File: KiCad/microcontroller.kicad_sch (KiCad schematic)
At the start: 11 parts, among them J1 Debugger, SW1 Reset switch, U1 STM32F051C6Tx, U7 24LC256

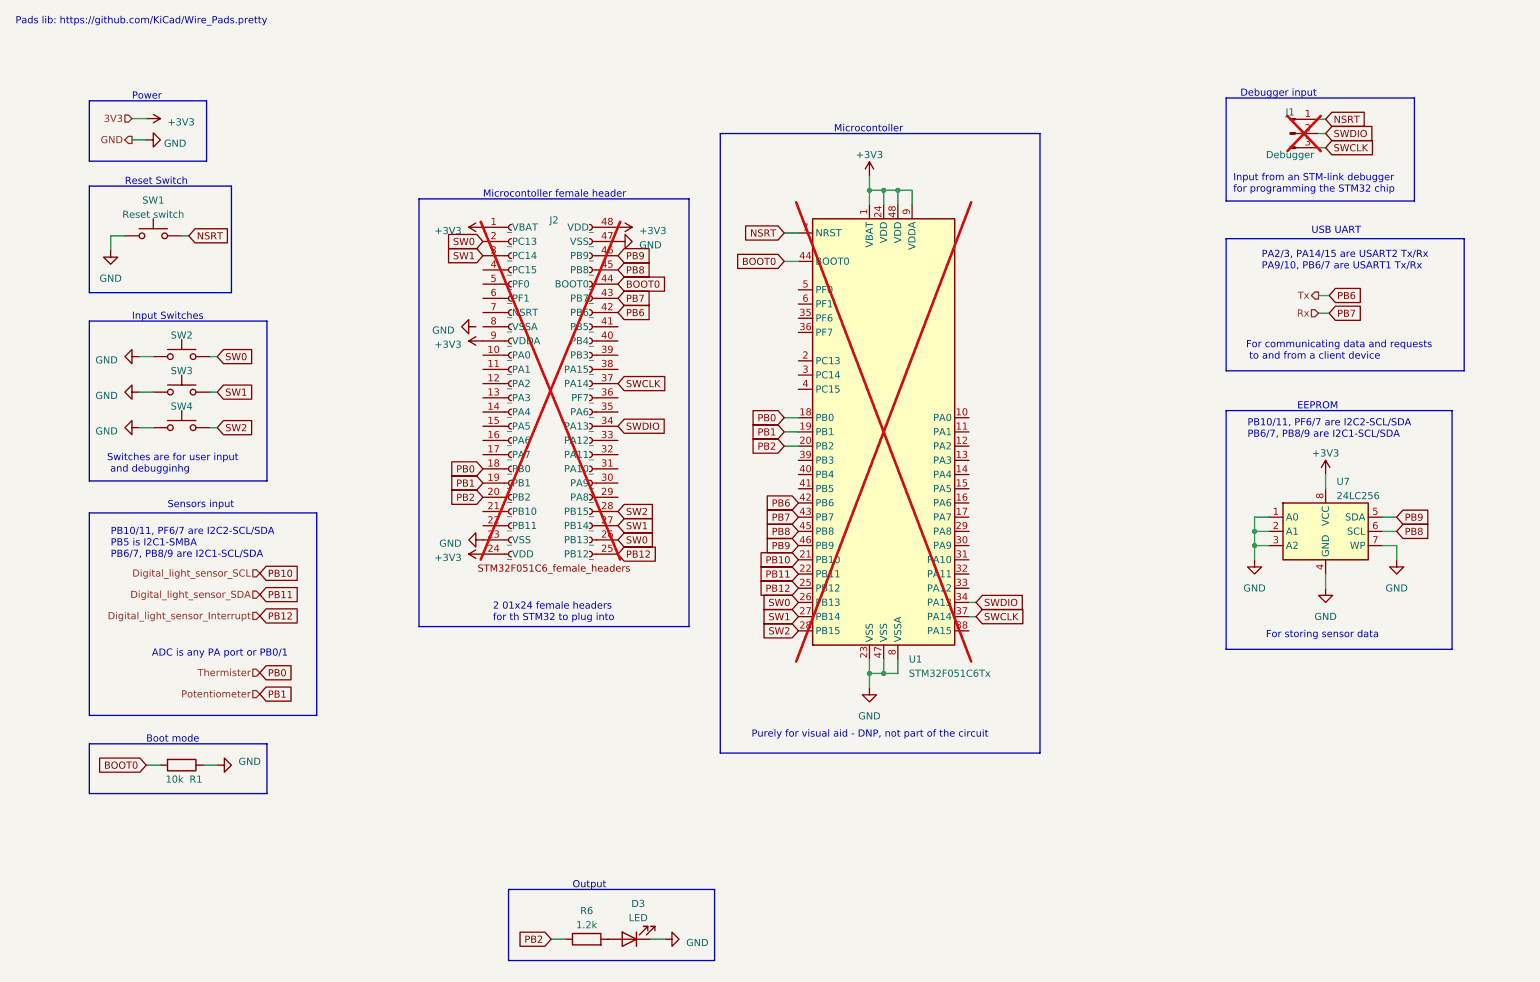
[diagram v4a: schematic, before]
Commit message: added failure mitigations and updated BOM
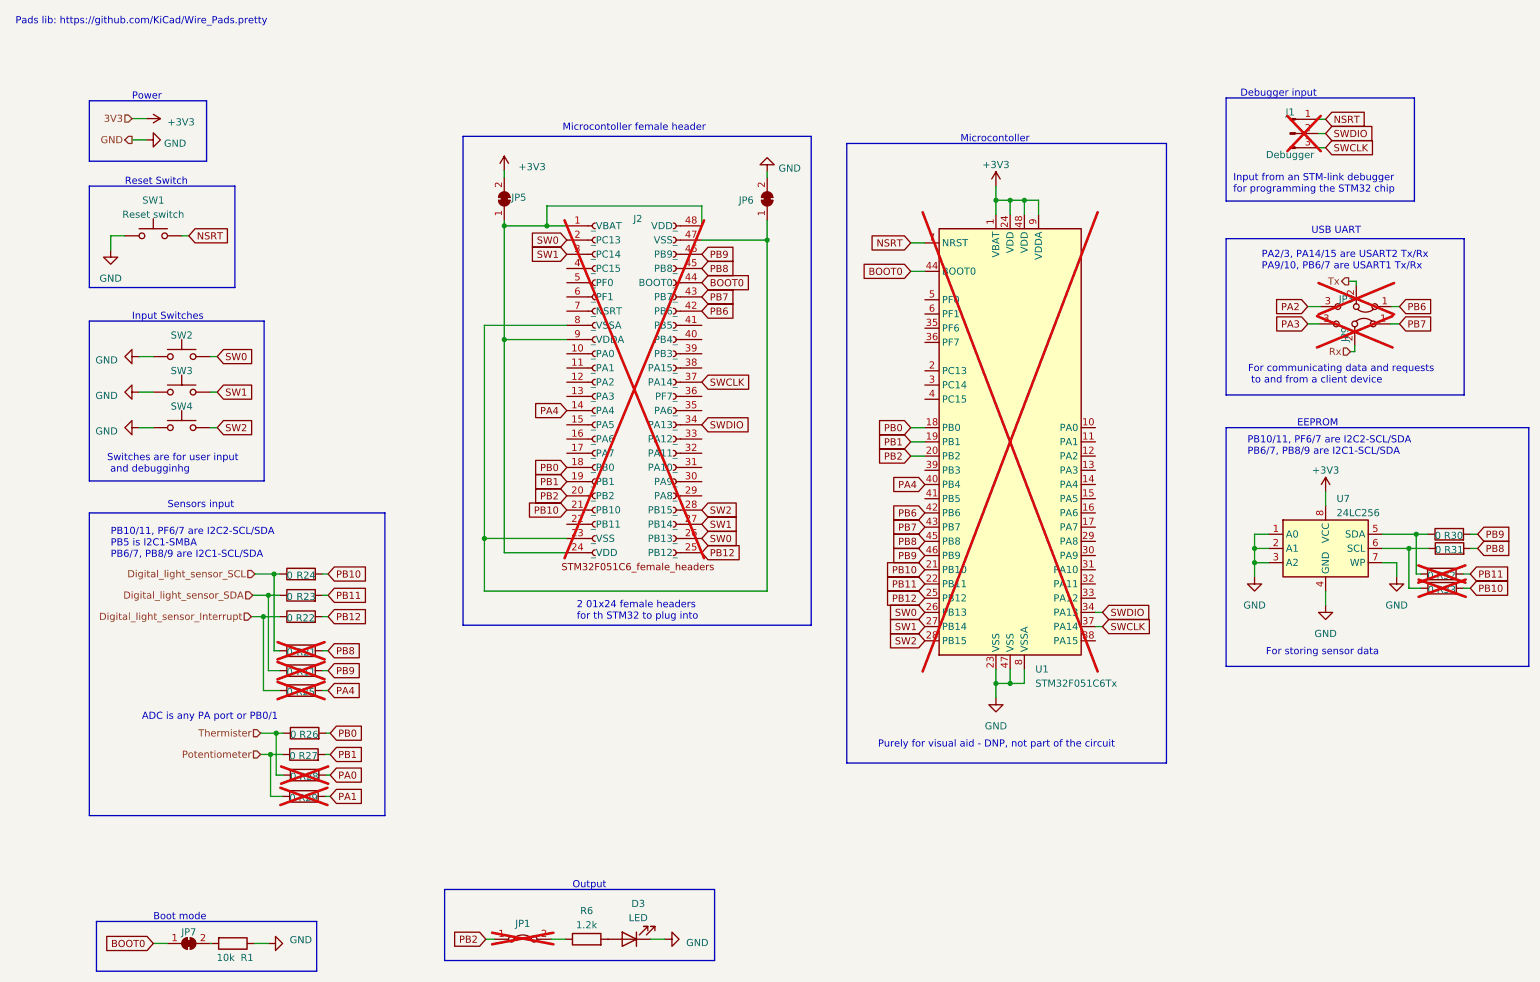
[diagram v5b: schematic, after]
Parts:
- added JP1: Jumper_2_Bridged, symbol Jumper:Jumper_2_Bridged
- added JP3, JP9: Jumper_3_Bridged12, symbol Jumper:Jumper_3_Bridged12
- added JP5, JP6, JP7: SolderJumper_2_Bridged, symbol Jumper:SolderJumper_2_Bridged
- added R11, R21, R22, R23, R24, R25, R26, R27, R28, R29, R30, R31, R32, R33: 0, symbol Device:R
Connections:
- net +3V3: now also JP5.2 (B); no longer J2.1 (_VBAT), J2.24 (_VDD), J2.48 (VDD_), J2.9 (_VDDA)
- net BOOT0: now also JP7.1 (A); no longer R1.2
- net GND: now also JP6.2 (B); no longer J2.23 (_VSS), J2.47 (VSS_)
- net PB0: now also R26.2
- net PB1: now also R27.2
- net PB10: now also J2.21 (_PB10), R24.2, R33.2
- net PB11: now also R23.2, R32.2
- net PB12: now also R22.2
- net PB2: now also JP1.1 (A); no longer R6.1
- net PB6: now also JP3.1 (A)
- net PB7: now also JP9.1 (A)
- net PB8: now also R21.2, R31.2; no longer U7.6 (SCL)
- net PB9: now also R11.2, R30.2; no longer U7.5 (SDA)
- net PA4: now reaches J2.14 (_PA4)
- net PA4: now also U1.40 (PB4), R25.2
- net at J2.8 (_VSSA): now also J2.23 (_VSS), J2.47 (VSS_), JP6.1 (A)
- new net: JP1.2 (B), R6.1
- new net: JP7.2 (B), R1.2
- new net: R30.1, R32.1, U7.5 (SDA)
- new net: R31.1, R33.1, U7.6 (SCL)
- new net: J2.1 (_VBAT), J2.24 (_VDD), J2.48 (VDD_), J2.9 (_VDDA), JP5.1 (A)
- new net Digital_light_sensor_Interrupt: R22.1, R25.1
- new net Digital_light_sensor_SCL: R21.1, R24.1
- new net Digital_light_sensor_SDA: R11.1, R23.1
- new net PA0: R28.2
- new net PA1: R29.2
- new net PA2: JP3.3 (B)
- new net PA3: JP9.3 (B)
- new net Potentiometer: R27.1, R29.1
- new net Rx: JP9.2 (C)
- new net Thermister: R26.1, R28.1
- new net Tx: JP3.2 (C)
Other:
- moved on the sheet: J2, R1, U1, U7

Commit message: updated sensor and microcontroller schematics
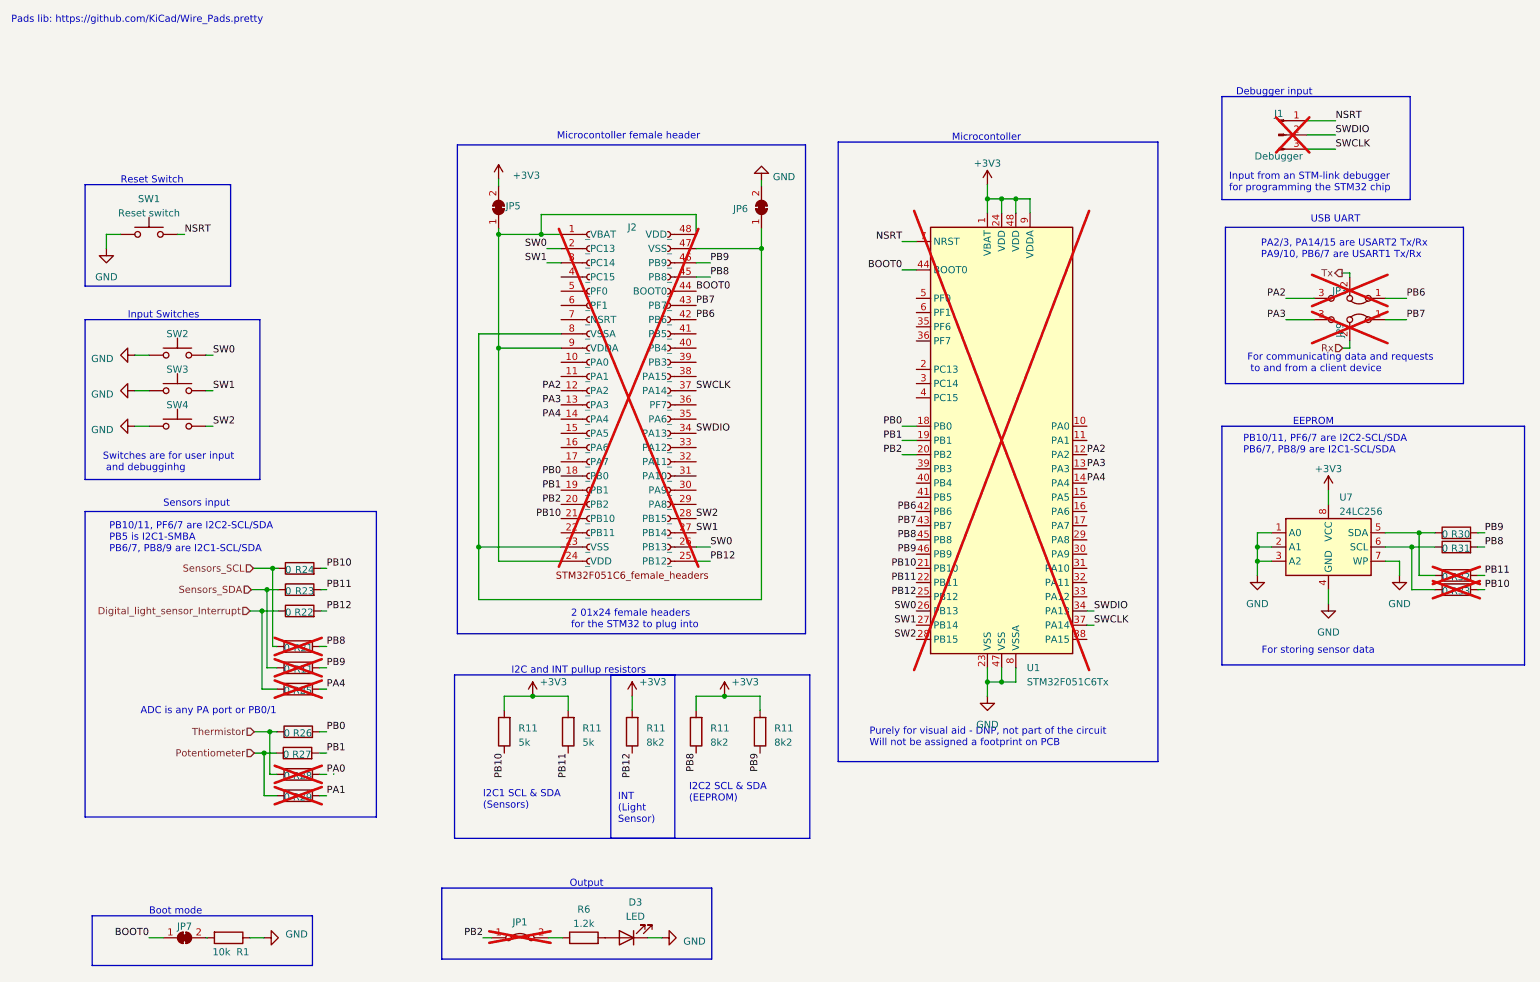
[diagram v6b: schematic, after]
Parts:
- added R11 (x2): 5k, symbol Device:R
- added R11 (x3): 8k2, symbol Device:R
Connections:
- net +3V3: now also R11.2, R11.2, R11.2, R11.2, R11.2
- net PA2: now also J2.12 (_PA2), U1.12 (PA2)
- net PA3: now also J2.13 (_PA3), U1.13 (PA3)
- net PA4: now also U1.14 (PA4); no longer U1.40 (PB4)
- net PB1: no longer R27.2
- net PB10: now also R11.1
- net PB11: now also R11.1
- net PB12: now also R11.1
- net PB8: now also R11.1
- net PB9: now also R11.1
- net Digital_light_sensor_SCL renamed Sensors_SCL
- net Digital_light_sensor_SDA renamed Sensors_SDA
- net Thermister renamed Thermistor
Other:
- note added: "2 01x24 female headers for the STM32 to plug into"
- note added: "I2C and INT pullup resistors"
- note added: "I2C1 SCL & SDA (Sensors)"
- note added: "I2C2 SCL & SDA (EEPROM)"
- note added: "INT (Light Sensor)"
- note added: "Purely for visual aid - DNP, not part of the circuit Will not be assigned a footprint on PCB"
- note removed: "2 01x24 female headers for th STM32 to plug into"
- note removed: "Power"
- note removed: "Purely for visual aid - DNP, not part of the circuit"
- moved on the sheet: D3, J1, J2, JP1, JP3, JP5, JP6, JP7, JP9, R1, R11, R21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

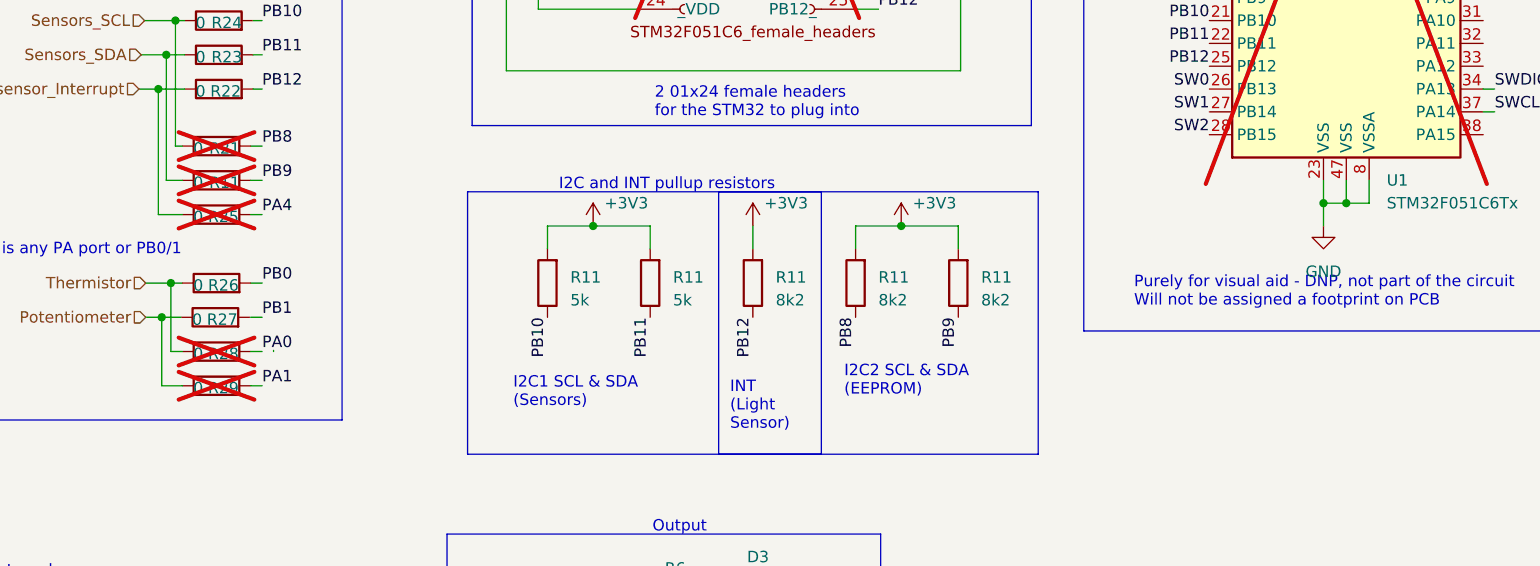
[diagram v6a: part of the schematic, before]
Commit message: edited circuit diagram in template design
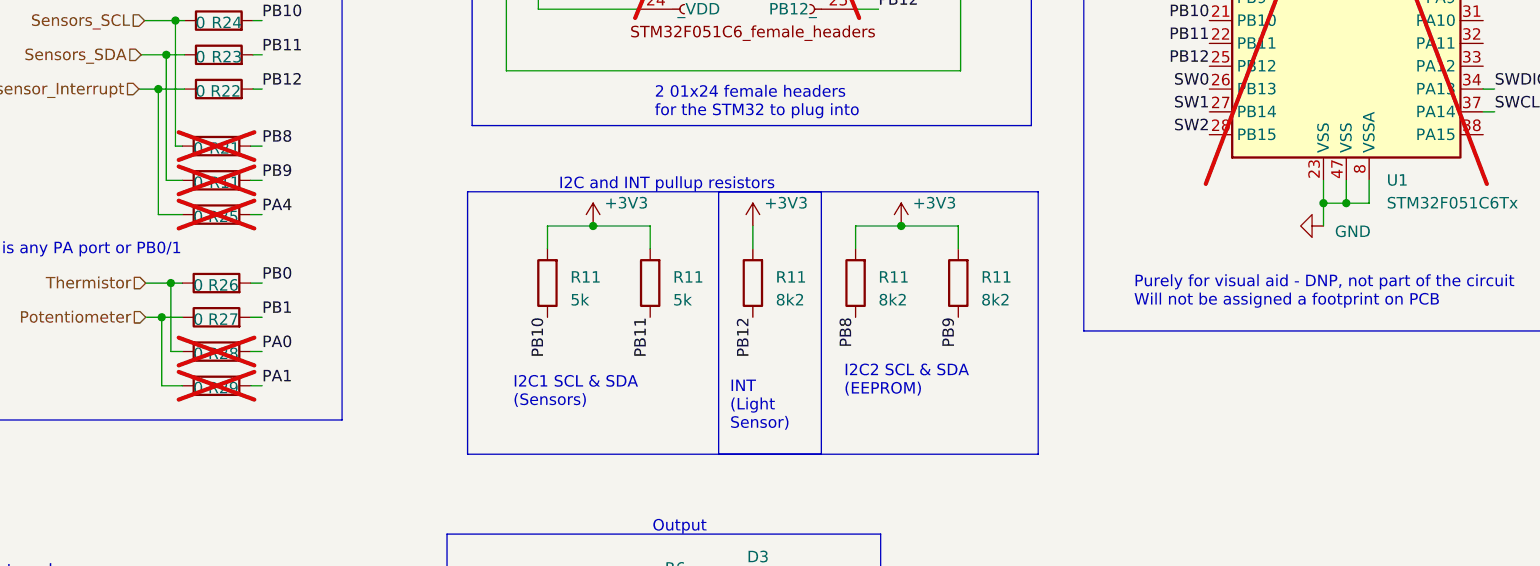
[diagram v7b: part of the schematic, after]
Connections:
- net PB1: now also R27.2
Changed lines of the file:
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@@
   (junction (at 234.95 110.49) (diameter 0) (color 0 0 0 0)
   )
+  (junction (at 57.404 144.78) (diameter 0) (color 0 0 0 0)
+  )
   (junction (at 99.314 72.39) (diameter 0) (color 0 0 0 0)
   )
-  (junction (at 57.404 144.78) (diameter 0) (color 0 0 0 0)
-  )
   (junction (at 95.758 107.95) (diameter 0) (color 0 0 0 0)
   )
@@
     (stroke (width 0) (type default))
   )
-  (wire (pts (xy 59.563 144.78) (xy 57.404 144.78))
-    (stroke (width 0) (type default))
-  )
   (wire (pts (xy 125.984 177.8) (xy 128.524 177.8))
     (stroke (width 0) (type default))
@@
     (stroke (width 0) (type default))
   )
-  (wire (pts (xy 69.85 148.59) (xy 69.85 148.463))
-    (stroke (width 0) (type default))
-  )
   (wire (pts (xy 57.404 177.8) (xy 54.864 177.8))
     (stroke (width 0) (type default))
@@
   )
   (wire (pts (xy 257.81 63.5) (xy 261.62 63.5))
+    (stroke (width 0) (type default))
+  )
+  (wire (pts (xy 57.404 144.78) (xy 59.69 144.78))
     (stroke (width 0) (type default))
   )
@@
     )
   )
-  (symbol (lib_id "power:GND") (at 186.69 134.62 0) (unit 1)
-    (in_bom yes) (on_board yes) (dnp no) (fields_autoplaced)
-    (property "Reference" "#PWR03" (at 186.69 140.97 0)
-      (effects (font (size 1.27 1.27)) hide)
-    )
-    (property "Value" "GND" (at 186.69 139.7 0)
-      (effects (font (size 1.27 1.27)))
+  (symbol (lib_id "power:GND") (at 186.69 134.62 270) (unit 1)
+    (in_bom yes) (on_board yes) (dnp no) (fields_autoplaced)
+    (property "Reference" "#PWR03" (at 180.34 134.62 0)
+      (effects (font (size 1.27 1.27)) hide)
+    )
+    (property "Value" "GND" (at 187.96 135.255 90)
+      (effects (font (size 1.27 1.27)) (justify left))
     )
     (property "Footprint" "" (at 186.69 134.62 0)
@@
     )
   )
-  (symbol (lib_id "Device:R") (at 63.373 144.78 90) (unit 1)
+  (symbol (lib_id "Device:R") (at 63.5 144.78 90) (unit 1)
     (in_bom yes) (on_board yes) (dnp no)
-    (property "Reference" "R27" (at 64.135 145.034 90)
-      (effects (font (size 1.27 1.27)))
-    )
-    (property "Value" "0" (at 61.341 145.034 90)
-      (effects (font (size 1.27 1.27)))
-    )
-    (property "Footprint" "" (at 63.373 146.558 90)
-      (effects (font (size 1.27 1.27)) hide)
-    )
-    (property "Datasheet" "~" (at 63.373 144.78 0)
-      (effects (font (size 1.27 1.27)) hide)
-    )
+    (property "Reference" "R27" (at 64.262 145.034 90)
+      (effects (font (size 1.27 1.27)))
+    )
+    (property "Value" "0" (at 61.468 145.034 90)
+      (effects (font (size 1.27 1.27)))
+    )
+    (property "Footprint" "" (at 63.5 146.558 90)
+      (effects (font (size 1.27 1.27)) hide)
+    )
+    (property "Datasheet" "~" (at 63.5 144.78 0)
+      (effects (font (size 1.27 1.27)) hide)
+    )
